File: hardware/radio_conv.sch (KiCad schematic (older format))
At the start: 15 parts, among them U701 WM8731, U702 MCP6L02

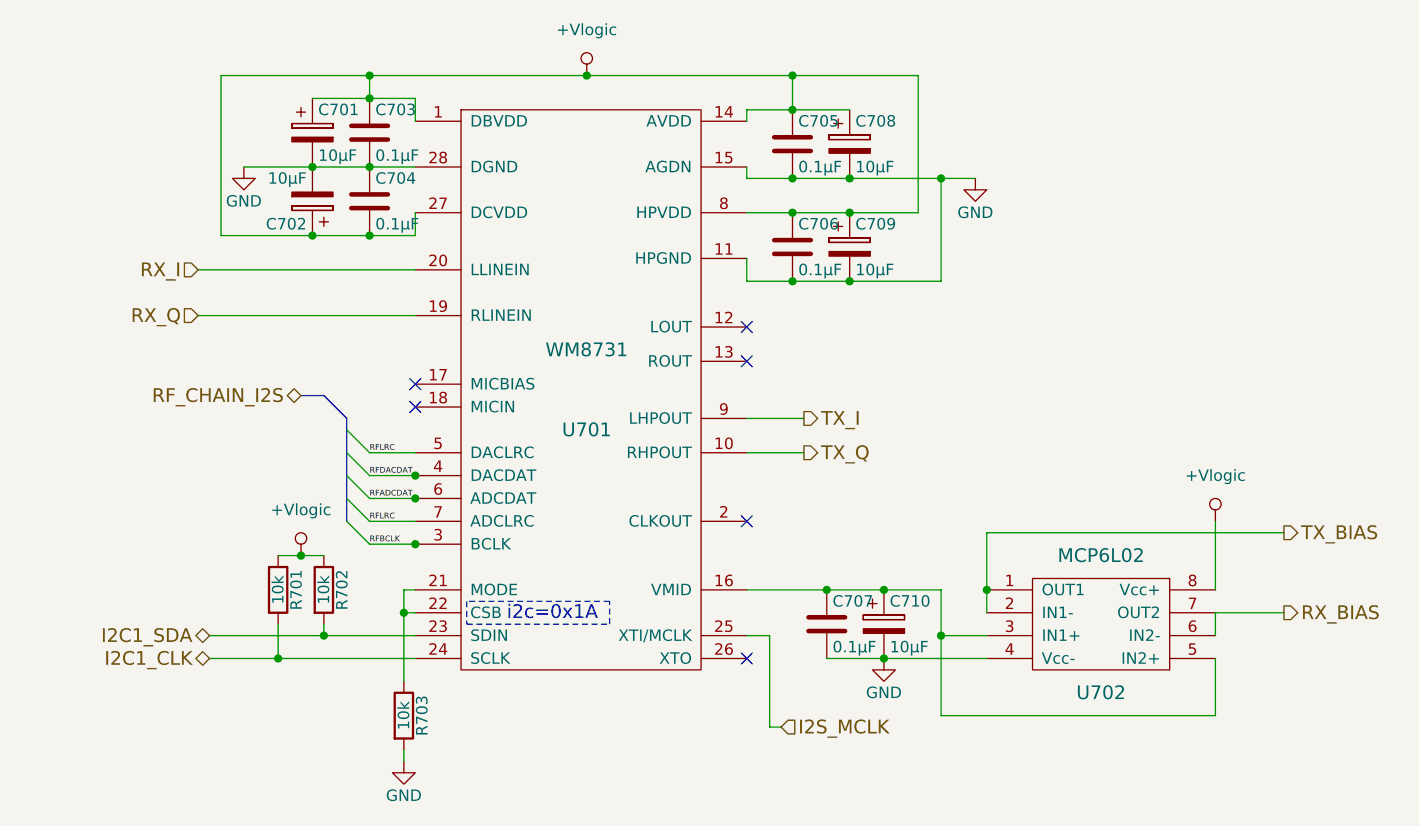
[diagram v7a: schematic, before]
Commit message: Upgraded schematic to version 1.0 and generated initial BOM
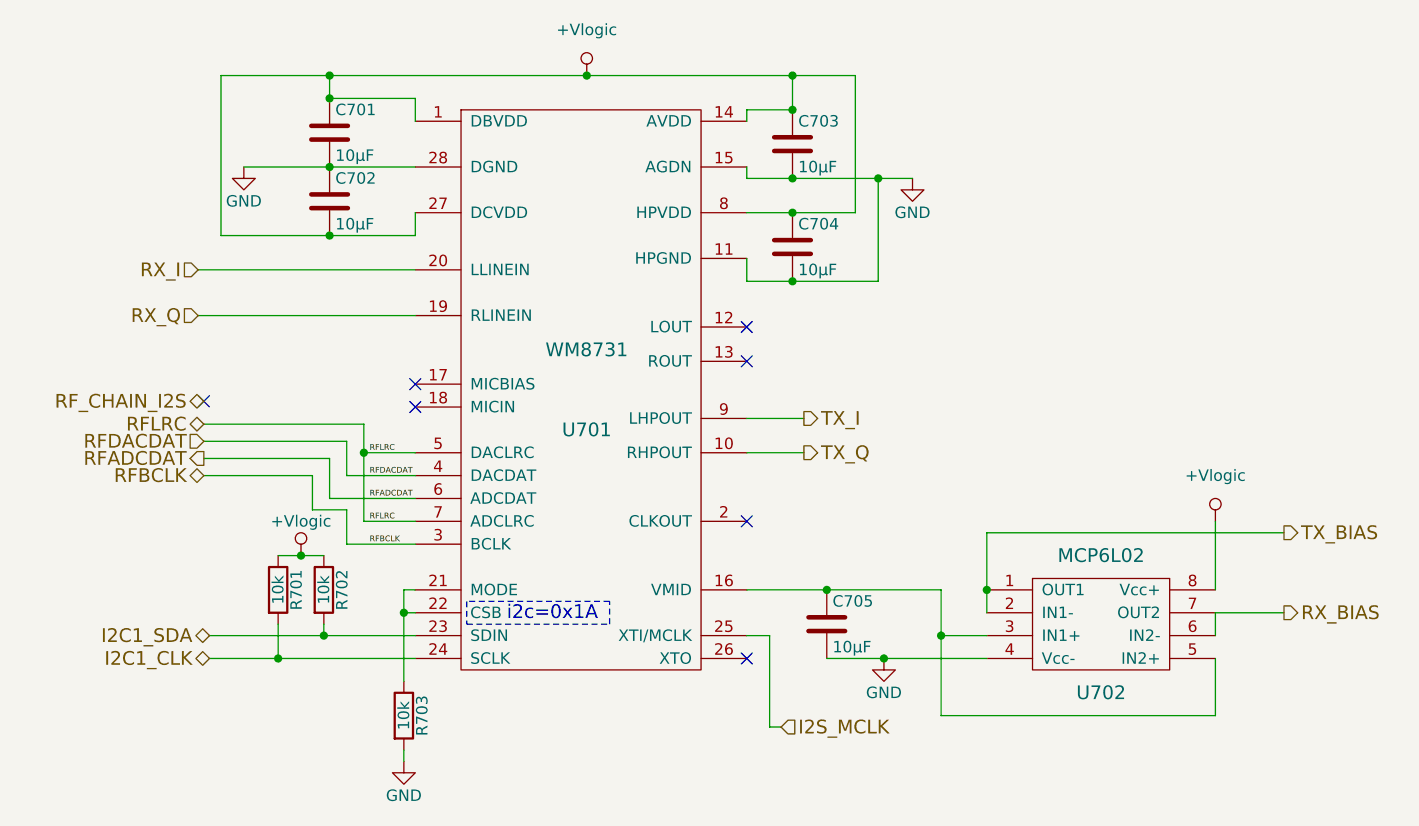
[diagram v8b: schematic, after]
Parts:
- removed C701, C702, C708, C709, C710: 10µF, symbol CP
- C701: renamed from C703; value 0.1µF -> 10µF
- C702: renamed from C704; value 0.1µF -> 10µF
- C703: renamed from C705; value 0.1µF -> 10µF
- C704: renamed from C706; value 0.1µF -> 10µF
- C705: renamed from C707; value 0.1µF -> 10µF
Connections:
- no-connect marks 6 -> 7
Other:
- moved on the sheet: C701, C702
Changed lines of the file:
@@
 Sheet 7 8
 Title "RF chain ADC/DAC"
-Date "2016-09-23"
-Rev "0.4"
+Date "2016-09-30"
+Rev "1.0"
 Comp "PRK - OH2TI"
 Comment1 "exla - OH2EHK"
@@
 $EndComp
 $Comp
-L +Vlogic #PWR046
+L +Vlogic #PWR704
 U 1 1 57E4C112
 P 5800 2200
-F 0 "#PWR046" H 5800 2000 50  0001 C CNN
+F 0 "#PWR704" H 5800 2000 50  0001 C CNN
 F 1 "+Vlogic" H 5800 2400 50  0000 C CNN
 F 2 "" H 5800 2200 50  0000 C CNN
@@
 $EndComp
 $Comp
-L CP C701
-U 1 1 57E4C118
-P 4600 2450
-F 0 "C701" H 4625 2550 50  0000 L CNN
-F 1 "10µF" H 4625 2350 50  0000 L CNN
-F 2 "" H 4638 2300 50  0000 C CNN
-F 3 "" H 4600 2450 50  0000 C CNN
-	1    4600 2450
-	1    0    0    -1
-$EndComp
-$Comp
-L CP C702
-U 1 1 57E4C11F
-P 4600 2750
-F 0 "C702" H 4625 2850 50  0000 L CNN
-F 1 "10µF" H 4625 2650 50  0000 L CNN
-F 2 "" H 4638 2600 50  0000 C CNN
-F 3 "" H 4600 2750 50  0000 C CNN
-	1    4600 2750
-	-1   0    0    1
-$EndComp
-$Comp
-L CP C710
-U 1 1 57E4C134
-P 7100 4600
-F 0 "C710" H 7125 4700 50  0000 L CNN
-F 1 "10µF" H 7125 4500 50  0000 L CNN
-F 2 "" H 7138 4450 50  0000 C CNN
-F 3 "" H 7100 4600 50  0000 C CNN
-	1    7100 4600
-	1    0    0    -1
-$EndComp
-$Comp
-L C C703
+L C C701
 U 1 1 57E4C13B
-P 4850 2450
-F 0 "C703" H 4875 2550 50  0000 L CNN
-F 1 "0.1µF" H 4875 2350 50  0000 L CNN
-F 2 "" H 4888 2300 50  0000 C CNN
-F 3 "" H 4850 2450 50  0000 C CNN
-	1    4850 2450
-	1    0    0    -1
-$EndComp
-$Comp
-L C C704
+P 4675 2450
+F 0 "C701" H 4700 2550 50  0000 L CNN
+F 1 "10µF" H 4700 2350 50  0000 L CNN
+F 2 "" H 4713 2300 50  0000 C CNN
+F 3 "" H 4675 2450 50  0000 C CNN
+	1    4675 2450
+	1    0    0    -1
+$EndComp
+$Comp
+L C C702
 U 1 1 57E4C142
-P 4850 2750
-F 0 "C704" H 4875 2850 50  0000 L CNN
-F 1 "0.1µF" H 4875 2650 50  0000 L CNN
-F 2 "" H 4888 2600 50  0000 C CNN
-F 3 "" H 4850 2750 50  0000 C CNN
-	1    4850 2750
-	1    0    0    -1
-$EndComp
-$Comp
-L GND #PWR047
+P 4675 2750
+F 0 "C702" H 4700 2850 50  0000 L CNN
+F 1 "10µF" H 4700 2650 50  0000 L CNN
+F 2 "" H 4713 2600 50  0000 C CNN
+F 3 "" H 4675 2750 50  0000 C CNN
+	1    4675 2750
+	1    0    0    -1
+$EndComp
+$Comp
+L GND #PWR701
 U 1 1 57E4C149
 P 4300 2600
-F 0 "#PWR047" H 4300 2350 50  0001 C CNN
+F 0 "#PWR701" H 4300 2350 50  0001 C CNN
 F 1 "GND" H 4300 2450 50  0000 C CNN
 F 2 "" H 4300 2600 50  0000 C CNN
@@
 Wire Wire Line
 	5050 2300 5050 2400
-Wire Wire Line
-	4600 2300 5050 2300
-Connection ~ 4850 2300
-Wire Wire Line
-	4850 2300 4850 2200
-Wire Wire Line
-	4200 2200 7250 2200
-Connection ~ 4600 2600
-Connection ~ 4850 2600
-$Comp
-L C C705
+Connection ~ 4675 2300
+Wire Wire Line
+	4675 2300 4675 2200
+Wire Wire Line
+	4200 2200 6975 2200
+Connection ~ 4675 2600
+$Comp
+L C C703
 U 1 1 57E4C15D
 P 6700 2500
-F 0 "C705" H 6725 2600 50  0000 L CNN
-F 1 "0.1µF" H 6725 2400 50  0000 L CNN
+F 0 "C703" H 6725 2600 50  0000 L CNN
+F 1 "10µF" H 6725 2400 50  0000 L CNN
 F 2 "" H 6738 2350 50  0000 C CNN
 F 3 "" H 6700 2500 50  0000 C CNN
@@
 $EndComp
 $Comp
-L C C706
+L C C704
 U 1 1 57E4C164
 P 6700 2950
-F 0 "C706" H 6725 3050 50  0000 L CNN
-F 1 "0.1µF" H 6725 2850 50  0000 L CNN
+F 0 "C704" H 6725 3050 50  0000 L CNN
+F 1 "10µF" H 6725 2850 50  0000 L CNN
 F 2 "" H 6738 2800 50  0000 C CNN
 F 3 "" H 6700 2950 50  0000 C CNN
@@
 Connection ~ 5800 2200
 Wire Wire Line
-	6500 2350 6950 2350
-Wire Wire Line
 	6500 2350 6500 2400
 Connection ~ 6700 2350
 Wire Wire Line
-	6500 2650 7500 2650
+	6500 2650 7225 2650
 Wire Wire Line
 	6500 2650 6500 2600
 Connection ~ 6700 2650
-Connection ~ 6950 2650
-$Comp
-L GND #PWR048
+$Comp
+L GND #PWR706
 U 1 1 57E4C178
-P 7500 2650
-F 0 "#PWR048" H 7500 2400 50  0001 C CNN
-F 1 "GND" H 7500 2500 50  0000 C CNN
-F 2 "" H 7500 2650 50  0000 C CNN
-F 3 "" H 7500 2650 50  0000 C CNN
-	1    7500 2650
-	1    0    0    -1
-$EndComp
-Wire Wire Line
-	7250 2200 7250 2800
-Wire Wire Line
-	7250 2800 6500 2800
+P 7225 2650
+F 0 "#PWR706" H 7225 2400 50  0001 C CNN
+F 1 "GND" H 7225 2500 50  0000 C CNN
+F 2 "" H 7225 2650 50  0000 C CNN
+F 3 "" H 7225 2650 50  0000 C CNN
+	1    7225 2650
+	1    0    0    -1
+$EndComp
+Wire Wire Line
+	6975 2200 6975 2800
+Wire Wire Line
+	6975 2800 6500 2800
 Connection ~ 6700 2200
-Connection ~ 6950 2800
 Connection ~ 6700 2800
 Wire Wire Line
 	6500 3000 6500 3100
 Wire Wire Line
-	6500 3100 7350 3100
-Wire Wire Line
-	7350 3100 7350 2650
-Connection ~ 7350 2650
+	6500 3100 7075 3100
+Wire Wire Line
+	7075 3100 7075 2650
+Connection ~ 7075 2650
 Connection ~ 6700 3100
 NoConn ~ 6500 3300
@@
 Wire Wire Line
 	5050 2900 5050 2800
-Connection ~ 4850 2900
+Connection ~ 4675 2900
 Wire Wire Line
 	4200 2900 4200 2200
-Connection ~ 4850 2200
-Connection ~ 4600 2900
-$Comp
-L +Vlogic #PWR049
+Connection ~ 4675 2200
+$Comp
+L +Vlogic #PWR702
 U 1 1 57E4C199
 P 4550 4300
-F 0 "#PWR049" H 4550 4100 50  0001 C CNN
-F 1 "+Vlogic" H 4550 4500 50  0000 C CNN
+F 0 "#PWR702" H 4550 4100 50  0001 C CNN
+F 1 "+Vlogic" H 4550 4450 50  0000 C CNN
 F 2 "" H 4550 4300 50  0000 C CNN
 F 3 "" H 4550 4300 50  0000 C CNN
@@
 Connection ~ 4550 4300
 $Comp
-L C C707
+L C C705
 U 1 1 57E4C1B6
 P 6850 4600
-F 0 "C707" H 6875 4700 50  0000 L CNN
-F 1 "0.1µF" H 6875 4500 50  0000 L CNN
+F 0 "C705" H 6875 4700 50  0000 L CNN
+F 1 "10µF" H 6875 4500 50  0000 L CNN
 F 2 "" H 6888 4450 50  0000 C CNN
 F 3 "" H 6850 4600 50  0000 C CNN
@@
 	6850 4750 7550 4750
 $Comp
-L GND #PWR050
+L GND #PWR705
 U 1 1 57E4C1C1
 P 7100 4750
-F 0 "#PWR050" H 7100 4500 50  0001 C CNN
+F 0 "#PWR705" H 7100 4500 50  0001 C CNN
 F 1 "GND" H 7100 4600 50  0000 C CNN
 F 2 "" H 7100 4750 50  0000 C CNN
@@
 	1    0    0    -1
 $EndComp
-Entry Wire Line
-	4750 4150 4850 4250
-Entry Wire Line
-	4750 4050 4850 4150
-Entry Wire Line
-	4750 3950 4850 4050
-Entry Wire Line
-	4750 3850 4850 3950
-Entry Wire Line
-	4750 3750 4850 3850
-Text HLabel 4550 3600 0    60   BiDi ~ 0
+Text HLabel 4125 3625 0    60   BiDi ~ 0
 RF_CHAIN_I2S
-Wire Bus Line
-	4650 3600 4750 3700
-Wire Bus Line
-	4750 3700 4750 4150
-Wire Bus Line
-	4650 3600 4550 3600
 Text HLabel 4150 4650 0    60   BiDi ~ 0
 I2C1_SDA
@@
 RX_Q
 $Comp
-L GND #PWR051
+L GND #PWR703
 U 1 1 57E4C1DF
 P 5000 5200
-F 0 "#PWR051" H 5000 4950 50  0001 C CNN
+F 0 "#PWR703" H 5000 4950 50  0001 C CNN
 F 1 "GND" H 5000 5050 50  0000 C CNN
 F 2 "" H 5000 5200 50  0000 C CNN
@@
 Wire Wire Line
 	7350 4650 7550 4650
-Connection ~ 7100 4450
 Wire Wire Line
 	7350 5000 8550 5000
@@
 	8550 4550 8550 4650
 $Comp
-L +Vlogic #PWR052
+L +Vlogic #PWR707
 U 1 1 57E46B0D
 P 8550 4150
-F 0 "#PWR052" H 8550 3950 50  0001 C CNN
+F 0 "#PWR707" H 8550 3950 50  0001 C CNN
 F 1 "+Vlogic" H 8550 4350 50  0000 C CNN
 F 2 "" H 8550 4150 50  0000 C CNN
@@
 	8550 4550 8850 4550
 Wire Wire Line
-	5050 3850 4850 3850
-Wire Wire Line
-	5050 3950 4850 3950
-Wire Wire Line
-	5050 4050 4850 4050
-Wire Wire Line
-	5050 4150 4850 4150
-Wire Wire Line
-	5050 4250 4850 4250
+	4825 3850 5050 3850
+Wire Wire Line
+	4750 3950 5050 3950
+Wire Wire Line
+	4675 4050 5050 4050
+Wire Wire Line
+	4825 4150 5050 4150
+Wire Wire Line
+	4750 4250 5050 4250
 Connection ~ 5000 4550
 Wire Wire Line
@@
 Wire Wire Line
 	5000 5200 5000 5150
-$Comp
-L CP C709
-U 1 1 57E4C12D
-P 6950 2950
-F 0 "C709" H 6975 3050 50  0000 L CNN
-F 1 "10µF" H 6975 2850 50  0000 L CNN
-F 2 "" H 6988 2800 50  0000 C CNN
-F 3 "" H 6950 2950 50  0000 C CNN
-	1    6950 2950
-	1    0    0    -1
-$EndComp
-$Comp
-L CP C708
-U 1 1 57E4C126
-P 6950 2500
-F 0 "C708" H 6975 2600 50  0000 L CNN
-F 1 "10µF" H 6975 2400 50  0000 L CNN
-F 2 "" H 6988 2350 50  0000 C CNN
-F 3 "" H 6950 2500 50  0000 C CNN
-	1    6950 2500
-	1    0    0    -1
-$EndComp
-Connection ~ 6950 3100
-Connection ~ 5050 4250
-Connection ~ 5050 4050
-Connection ~ 5050 3950
+Wire Wire Line
+	5050 2300 4675 2300
+Wire Wire Line
+	6700 2350 6500 2350
+NoConn ~ 4125 3625
+Text HLabel 4125 3725 0    60   BiDi ~ 0
+RFLRC
+Text HLabel 4125 3800 0    60   Input ~ 0
+RFDACDAT
+Text HLabel 4125 3875 0    60   Output ~ 0
+RFADCDAT
+Text HLabel 4125 3950 0    60   BiDi ~ 0
+RFBCLK
+Wire Wire Line
+	4825 3725 4825 4150
+Wire Wire Line
+	4825 3725 4125 3725
+Wire Wire Line
+	4750 3950 4750 3800
+Wire Wire Line
+	4750 3800 4125 3800
+Wire Wire Line
+	4125 3875 4675 3875
+Wire Wire Line
+	4675 3875 4675 4050
+Connection ~ 4825 3850
+Wire Wire Line
+	4750 4250 4750 4100
+Wire Wire Line
+	4750 4100 4600 4100
+Wire Wire Line
+	4600 4100 4600 3950
+Wire Wire Line
+	4600 3950 4125 3950
 $EndSCHEMATC
